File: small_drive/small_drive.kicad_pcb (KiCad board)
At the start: 2 copper layers, 83.8 x 71.8 mm, 143 parts, among them CON1 BARREL_JACK, J1 DB9, M1 SiR826DP, M2 SiR826DP, M3 SiR826DP, M4 SiR826DP, M5 SiR826DP, M6 SiR826DP, M7 SiR826DP, P1 CONN_01X04, P10 CONN_01X02, P11 CONN_01X02, P12 CONN_01X02, P13 CONN_01X04, P14 CONN_01X02, P2 CONN_01X04, P3 CONN_01X06, P4 CONN_01X08, P5 CONN_01X02, P6 CONN_01X02, P7 CONN_01X02, P8 CONN_01X02, P9 CONN_01X04, U1 STM32F334K8, U10 LM5106, U11 ACS711ELCTR-25AB-T, U12 ACS711ELCTR-25AB-T, U13 ACS711ELCTR-25AB-T, U14 STM32F030F4P6TR, U15 LTC2850, U16 LIS3LV02DQ, U17 STM32F030F4P6TR, U18 LTC2850, U19 LIS3LV02DQ, U2 OKR_T3, U20 DS28CM00, U21 DS28CM00, U22 TL431, U23 LT3012, U24 STM32F030F4P6TR, U25 MC33074DTBR2, U3 LTC2850, U4 LTC2850, U5 LTC2850, U6 LT1764EQ, U7 MC33074DTBR2, U8 LM5106, U9 LM5106

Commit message: Before splitting.
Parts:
- added C48: C, Capacitors_SMD:C_0603, B.Cu at (108.2, 88.5)
- added C49: C, Capacitors_SMD:C_0603, B.Cu at (108.2, 87.0)
- added Y1: Crystal, Crystals:QC3CA, B.Cu at (111.8, 88.5)
- moved C16 3.18 mm to (108.2, 90.0), turned to 180 degrees
- moved P13 1.50 mm to (170.5, 112.3)
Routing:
- net Net-(C49-Pad2): track 0.00 -> 9.74 mm
- net Net-(C48-Pad2): track 0.00 -> 8.62 mm
- net /A: track 37.8 -> 43.8 mm
- net /B: track 33.8 -> 39.4 mm
- net /pomp/Vdd: track 76.6 -> 81.8 mm
- net /Z: track 31.4 -> 36.5 mm
- net GND: track 365.1 -> 369.6 mm
- net +12V: track 139.5 -> 143.8 mm
- net /pomp/SWCLK: track 11.6 -> 12.8 mm
- net /pomp/Vss: track 169.0 -> 169.7 mm
- net Net-(C47-Pad1): track 2.66 -> 3.32 mm
- net /pomp/SWDIO: track 9.94 -> 10.6 mm
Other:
- board text added: "0"
- board text added: "0 D C +3.3"
- board text added: "SWD C,D"

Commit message: PCB ordered
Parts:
- removed C10, C11, C28, C29, C30, C31, C32, C33, C34, C35, C36, C37, C38, C40, C42, C43, C44: 100nF, Capacitors_SMD:C_0603
- removed C39: 470uF/63V, Capacitors_ThroughHole:C_Radial_D16_L25_P7.5
- removed C41: 100uF/35V, Capacitors_SMD:c_elec_8x10.5
- removed C45: 1uF/100V, Capacitors_SMD:C_1206
- removed C46: C, Capacitors_SMD:C_0603
- removed D5, D6, D7, D8: STPS2150A, Diodes_SMD:SMA_Standard
- removed HOLE5, HOLE6, HOLE7, HOLE8: HOLE, Mounting_Holes:MountingHole_3mm
- removed M7: SiR826DP, 00_Passives:SOT-669_GDS
- removed P1, P9: CONN_01X04, Pin_Headers:Pin_Header_Angled_1x04
- removed P10, P8: CONN_01X02, Pin_Headers:Pin_Header_Straight_1x02
- removed P11, P12, P14: CONN_01X02, 00_Passives:Wiecon_25.197.0253.0
- removed P13: CONN_01X04, Pin_Headers:Pin_Header_Straight_1x04
- removed R18, R19: R, Resistors_SMD:R_0603
- removed R20: 1.5k, Resistors_SMD:R_0603
- removed R21: 300, Resistors_SMD:R_0603
- removed R22: 910, Resistors_SMD:R_0603
- removed R23, R29, R30, R31: 1k, Resistors_SMD:R_0603
- removed R24: 3.0k, Resistors_SMD:R_0603
- removed R25: 1.8k, Resistors_SMD:R_0603
- removed R26: 51k, Resistors_SMD:R_0603
- removed R27: 2.2k, Resistors_SMD:R_0603
- removed R28: R, Resistors_SMD:R_2512
- removed U14, U17, U24: STM32F030F4P6TR, Housings_SSOP:TSSOP-20_4.4x6.5mm_Pitch0.65mm
- removed U15, U18: LTC2850, Housings_SOIC:SOIC-8_3.9x4.9mm_Pitch1.27mm
- removed U16, U19: LIS3LV02DQ, Housings_DFN_QFN:QFN-28-1EP_7x7mm_Pitch0.8mm
- removed U20, U21: DS28CM00, 00_Passives:SOT23_5
- removed U22: TL431, TO_SOT_Packages_SMD:SOT-23
- removed U23: LT3012, Housings_SSOP:TSSOP-16-1EP_4.4x5mm_Pitch0.65mm
- removed U25: MC33074DTBR2, Housings_SSOP:TSSOP-14_4.4x5mm_Pitch0.65mm
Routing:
- net /pomp/Vss: track 169.7 -> 0.00 mm, vias 1 -> 0
- net /pomp/Vdd: track 81.8 -> 0.00 mm, vias 1 -> 0
- net /g_sensor2/Vss: track 79.3 -> 0.00 mm, vias 2 -> 0
- net /g_sensor1/Vss: track 79.3 -> 0.00 mm, vias 2 -> 0
- net /pomp/Vpower: track 69.4 -> 0.00 mm
- net /g_sensor1/Vdd: track 59.6 -> 0.00 mm, vias 2 -> 0
- net /g_sensor2/Vdd: track 59.6 -> 0.00 mm, vias 2 -> 0
- net /pomp/MAINS: track 39.0 -> 0.00 mm
- net /pomp/CURRENT: track 16.0 -> 0.00 mm
- net Net-(C38-Pad1): track 14.3 -> 0.00 mm
- net Net-(D7-PadA): track 13.8 -> 0.00 mm
- net /pomp/SWCLK: track 12.8 -> 0.00 mm
- net Net-(M7-PadS): track 12.5 -> 0.00 mm
- net /pomp/SWDIO: track 10.6 -> 0.00 mm
- net Net-(R26-Pad2): track 10.4 -> 0.00 mm
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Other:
- board size 83.8 x 71.8 mm -> 58.8 x 71.8 mm
- board text removed: "0"
- board text removed: "0 D C +3.3"
- board text removed: "SWD C,D"

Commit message: Pauze klus.
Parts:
- removed CON1: BARREL_JACK, 00_Passives:smd_barrel_jack
- removed P4: CONN_01X08, Connectors_Molex:Molex_PicoBlade_53261-0871
- added C10: 100nF, Capacitors_SMD:C_0603, F.Cu at (68.5, 79.2)
- added C11: 100nF, Capacitors_SMD:C_0603, F.Cu at (71.0, 76.8)
- added C28: 100nF, Capacitors_SMD:C_0603, F.Cu at (72.5, 83.2)
- added C29: 100nF, Capacitors_SMD:C_0603, F.Cu at (75.0, 80.2)
- added C30: 10uF, Capacitors_SMD:C_1210, F.Cu at (68.2, 75.0)
- added C31: 10uF, Capacitors_SMD:C_1210, F.Cu at (75.0, 85.2)
- added C32: 100uF/35V, Capacitors_SMD:c_elec_8x10.5, F.Cu at (69.0, 59.0)
- added C33: 100nF, Capacitors_SMD:C_0603, B.Cu at (72.2, 56.2)
- added C34: 100uF/35V, Capacitors_SMD:c_elec_8x10.5, F.Cu at (114.0, 53.5)
- added C35: 10nF, Capacitors_SMD:C_0603, F.Cu at (113.0, 68.2)
- added C36: 100uF/35V, Capacitors_SMD:c_elec_8x10.5, F.Cu at (125.0, 53.5)
- added C37: 100nF, Capacitors_SMD:C_0603, F.Cu at (107.2, 59.0)
- added C38: 100uF/35V, Capacitors_SMD:c_elec_8x10.5, F.Cu at (67.8, 116.5)
- added C39: 100nF, Capacitors_SMD:C_0603, F.Cu at (107.0, 76.0)
- added C40: 100nF, Capacitors_SMD:C_0603, F.Cu at (107.0, 94.5)
- added C41: 100nF, Capacitors_SMD:C_0603, F.Cu at (107.0, 113.0)
- added C42: 100nF, Capacitors_SMD:C_0603, F.Cu at (75.5, 88.5)
- added C43: 100nF, Capacitors_SMD:C_0603, F.Cu at (98.5, 95.5)
- added C44: 2.2uF, Capacitors_SMD:C_1206, B.Cu at (74.8, 95.0)
- added C45: 100nF, Capacitors_SMD:C_0603, F.Cu at (72.2, 91.2)
- added C46: 25pF, Capacitors_SMD:C_0603, F.Cu at (67.0, 91.0)
- added C50: 100nF, Capacitors_SMD:C_0603, B.Cu at (69.8, 102.8)
- added C51: 100nF, Capacitors_SMD:C_0603, B.Cu at (69.8, 99.0)
- added C52: 100nF, Capacitors_SMD:C_0603, F.Cu at (116.2, 125.0)
- added C53: 100nF, Capacitors_SMD:C_0603, F.Cu at (116.2, 82.2)
- added C54: 100nF, Capacitors_SMD:C_0603, F.Cu at (116.2, 100.8)
- added C55: 100nF, Capacitors_SMD:C_0603, F.Cu at (116.2, 119.2)
- added C56: 100nF, Capacitors_SMD:C_0603, F.Cu at (32.4, 67.6)
- added C57: 100nF, Capacitors_SMD:C_0603, B.Cu at (57.8, 102.5)
- added C58: 100nF, Capacitors_SMD:C_0603, F.Cu at (37.5, 67.6)
- added C59: 100nF, Capacitors_SMD:C_0603, B.Cu at (66.2, 66.8)
- added J2: DB15, Connectors_Amphenol:DB15F_HD20_SIZE2, F.Cu at (58.0, 68.8)
- added P1: CONN_01X04, Connect:bornier4, F.Cu at (78.0, 130.5)
- added R18: 510, Resistors_SMD:R_0603, B.Cu at (59.8, 81.2)
- added R19: 1k, Resistors_SMD:R_0603, B.Cu at (54.5, 60.0)
- added R20: 1k, Resistors_SMD:R_0603, B.Cu at (61.5, 67.0)
- added R21: R, Resistors_SMD:R_0603, B.Cu at (61.8, 70.2)
- added R22: R, Resistors_SMD:R_0603, B.Cu at (62.5, 57.5)
- added R23: R, Resistors_SMD:R_0603, B.Cu at (62.5, 63.2)
- added R24: R, Resistors_SMD:R_0603, B.Cu at (58.2, 100.0)
- added R25: 1k, Resistors_SMD:R_0603, F.Cu at (100.2, 73.0)
- added R26: 1k, Resistors_SMD:R_0603, F.Cu at (102.0, 73.0)
- added R27: 510, Resistors_SMD:R_0603, F.Cu at (103.8, 73.0)
- added R28: 510, Resistors_SMD:R_0603, F.Cu at (105.5, 73.0)
- added R29: 680, Resistors_SMD:R_0603, F.Cu at (106.2, 131.5)
- added R30: 680, Resistors_SMD:R_0603, F.Cu at (106.2, 128.0)
- added R31: 680, Resistors_SMD:R_0603, F.Cu at (106.2, 129.8)
- added R33: 300, Resistors_SMD:R_0603, F.Cu at (114.5, 68.2)
- added R34: 56k, Resistors_SMD:R_0603, F.Cu at (114.5, 71.0)
- added R35: 6.49k, Resistors_SMD:R_0603, F.Cu at (67.0, 89.2)
- added R36: 220, Resistors_SMD:R_0603, B.Cu at (73.2, 92.5)
- added R37: 220, Resistors_SMD:R_0603, B.Cu at (81.0, 94.5)
- added R38: R, Resistors_SMD:R_0603, B.Cu at (57.8, 105.2)
- added R39: R, Resistors_SMD:R_0603, B.Cu at (50.8, 109.0)
- added R40: R, Resistors_SMD:R_0603, B.Cu at (49.8, 94.8)
- added R41: R, Resistors_SMD:R_0603, B.Cu at (54.0, 109.0)
- added R42: R, Resistors_SMD:R_0603, B.Cu at (55.0, 110.8)
- added R43: R, Resistors_SMD:R_0603, B.Cu at (49.8, 96.5)
- added R44: 22, Resistors_SMD:R_0603, B.Cu at (79.8, 84.2)
- added R45: 22, Resistors_SMD:R_0603, B.Cu at (79.8, 82.5)
- added R46: R, Resistors_SMD:R_0603, B.Cu at (74.2, 123.5)
- added U14: AD8226, Housings_SOIC:SOIC-8_3.9x4.9mm_Pitch1.27mm, B.Cu at (67.8, 63.2)
- added U15: MAX3096, Housings_SOIC:SOIC-16_3.9x9.9mm_Pitch1.27mm, B.Cu at (53.0, 102.8)
- added U16: AMC1203, 00_Passives:SO8_11, F.Cu at (105.5, 68.2)
- added U17: 7805, 00_Local:TO220_78xx, F.Cu at (124.8, 62.8)
- added U18: LT1764EQ, 00_Passives:DD-PAK, B.Cu at (66.2, 119.2)
- added U19: KSZ8081, Housings_DFN_QFN:QFN-24-1EP_4x4mm_Pitch0.5mm, B.Cu at (69.8, 91.0)
- added U20: ETH100_MAG, 00_Passives:ETH100_MAG, F.Cu at (68.1, 106.5)
- added X1: NKE1212DC, 00_Local:NKE-SC, F.Cu at (76.0, 55.0)
- added X2: NKE1212DC, 00_Local:NKE-SC, F.Cu at (111.5, 63.5)
- added X3: HCPL0201, Housings_SOIC:SOIC-8_3.9x4.9mm_Pitch1.27mm, F.Cu at (111.5, 82.2)
- added X4: HCPL0201, Housings_SOIC:SOIC-8_3.9x4.9mm_Pitch1.27mm, F.Cu at (111.5, 119.2)
- added X5: HCPL0201, Housings_SOIC:SOIC-8_3.9x4.9mm_Pitch1.27mm, F.Cu at (111.5, 100.8)
- added X6: HCPL0201, Housings_SOIC:SOIC-8_3.9x4.9mm_Pitch1.27mm, F.Cu at (111.5, 125.0)
- added Y2: 25MHz, Crystals:crystal_FA238-TSX3225, F.Cu at (64.0, 91.8)
- C13, C15, C16, C17, C18, C8, C9, R10, R11, R12, R13, R14, R6, R7, R8, R9, U12, U7: moved to F.Cu
- C47: value 100nF -> 25pF
- C48, C49: value C -> 15pF
- J1: footprint Connect:DB9FC -> Connectors_Amphenol:DB9FC_HD-20
- M1, M2, M3, M4, M5, M6: footprint 00_Passives:SOT-669_GDS -> 00_Passives:SOT-669_GDS_therma
- P3: value CONN_01X06 -> CONN_01X04; footprint Connectors_Molex:Molex_PicoBlade_53261-0671 -> Pin_Headers:Pin_Header_Straight_1x04; moved to F.Cu
- R1: value 270 -> 10k; moved to F.Cu
- R15, R16, R17: value R -> 10k
- R32: value 0 -> 680
- U1: value STM32F334K8 -> XMC4400-F64x512; footprint Housings_QFP:LQFP-32_7x7mm_Pitch0.8mm -> Housings_QFP:LQFP-64-1EP_10x10mm_Pitch0.5mm
- U11, U13: value ACS711ELCTR-25AB-T -> ACS711KLCTR-12AB-T; moved to F.Cu
- U2: value OKR_T3 -> ips511g; footprint 00_Passives:okr_t3 -> Housings_SOIC:SOIC-8_3.9x4.9mm_Pitch1.27mm; moved to B.Cu
- U3: value LTC2850 -> ips511g
- U5: value LTC2850 -> AD8226
- Y1: value Crystal -> 12MHz
- moved C17 87.5 mm to (68.5, 81.2)
- moved C3 79.0 mm to (50.8, 61.8), turned to 0 degrees
- moved C1 77.5 mm to (69.0, 68.0)
- moved U2 72.2 mm to (52.2, 71.0), turned to 180 degrees
- moved C18 71.3 mm to (75.0, 82.2), turned to 180 degrees
- moved C15 68.1 mm to (71.0, 83.2), turned to 90 degrees
- moved U5 63.7 mm to (67.8, 57.5), turned to 0 degrees
- moved C7 62.3 mm to (50.8, 74.5), turned to 0 degrees
- moved U3 55.6 mm to (52.2, 65.4)
- moved C14 55.1 mm to (67.8, 135.0), turned to 0 degrees
- moved J1 53.9 mm to (55.8, 127.9), turned to 270 degrees
- moved R1 53.2 mm to (68.5, 77.5), turned to 180 degrees
- moved C8 50.0 mm to (72.5, 76.8), turned to 270 degrees
- moved Y1 49.3 mm to (62.8, 82.8)
- moved U4 49.3 mm to (66.5, 70.2)
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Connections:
- C19 pad 1: GND -> GNDPWR
- C19 pad 2: +12V -> +12P
- C2 pad 2: GND -> GNDPWR
- C20 pad 1: GND -> GNDPWR
- C20 pad 2: +12V -> +12P
- C21 pad 1: GND -> GNDPWR
- C21 pad 2: +12V -> +12P
- C25 pad 2: GND -> GNDPWR
- C26 pad 2: GND -> GNDPWR
- C27 pad 2: GND -> GNDPWR
- C4 pad 2: GND -> GNDPWR
- C48 pad 1: GND -> Net-(C48-Pad1)
- C48 pad 2: Net-(C48-Pad2) -> GND
- C5 pad 2: GND -> GNDPWR
- C9 pad 1: +5V -> +3.3V
- D2 pad A: +12V -> +12P
- D3 pad A: +12V -> +12P
- D4 pad A: +12V -> +12P
- M2 pad S: GND -> GNDPWR
- M4 pad S: GND -> GNDPWR
- M6 pad S: GND -> GNDPWR
- P2 pad 1: +5V -> +3.3V
- P2 pad 2: /SWDAT -> Net-(P2-Pad2)
- P2 pad 3: /SWCLK -> Net-(P2-Pad3)
- P3 pad 1: GND -> /LED0
- P3 pad 2: GND -> /LED1
- P3 pad 3: Net-(P3-Pad3) -> /LED2
- P3 pad 4: Net-(P3-Pad4) -> /LED3
- P5 pad 1: +60V -> /M0
- P5 pad 2: /M0 -> +60V
- P6 pad 1: GND -> /M1
- P6 pad 2: /M1 -> GNDPWR
- P7 pad 1: GND -> /M2
- P7 pad 2: /M2 -> GNDPWR
- R1 pad 1: Net-(R1-Pad1) -> +3.3V
- R1 pad 2: GND -> Net-(R1-Pad2)
- R12 pad 1: +3.3V -> +3.3VADC
- R15 pad 2: GND -> GNDPWR
- R16 pad 2: GND -> GNDPWR
- R17 pad 2: GND -> GNDPWR
- R2 pad 1: Net-(D1-Pad6) -> Net-(D1-Pad8)
- R3 pad 1: Net-(D1-Pad8) -> Net-(D1-Pad2)
- R32 pad 1: +3.3V -> Net-(R32-Pad1)
- R32 pad 2: Net-(J1-Pad4) -> /HBEN
- R4 pad 1: Net-(D1-Pad2) -> Net-(D1-Pad6)
- R6 pad 1: +3.3V -> +3.3VADC
- R9 pad 1: +3.3V -> +3.3VADC
- U1 pad 1: +3.3V -> /ETH_CRS_DVA
- U1 pad 10: /CUR1 -> Net-(U1-Pad10)
- U1 pad 11: /CUR2 -> Net-(U1-Pad11)
- U1 pad 12: /LED0 -> Net-(U1-Pad12)
- U1 pad 13: /LED1 -> +3.3V
- U1 pad 14: /LED2 -> /ENC_SIN
- U1 pad 15: /LED3 -> /ENC_SIN
- U1 pad 16: GND -> /ENC_COS
- U1 pad 17: +3.3V -> Net-(U1-Pad17)
- U1 pad 18: /HB0 -> /CUR2
- U1 pad 19: /HB1 -> Net-(U1-Pad19)
- U1 pad 2: Net-(C48-Pad2) -> /ENC_RXD2
- U1 pad 20: /HB2 -> /CUR0
- U1 pad 21: /HBEN -> GND
- U1 pad 22: /DXD -> +3.3VADC
- U1 pad 23: /SWDAT -> Net-(U1-Pad23)
- U1 pad 24: /SWCLK -> /CUR1
- U1 pad 25: /ENC_RXD -> /VddC
- U1 pad 26: /ENC_TXD -> +3.3V
- U1 pad 27: Net-(U1-Pad27) -> /ETH0_TXD1
- U1 pad 28: /DXD -> /ETH0_TXD0
- U1 pad 29: /TXD -> /ETH0_TX_EN
- U1 pad 3: Net-(C49-Pad2) -> /LED2
- U1 pad 30: /RXD -> /ETH0_RXERA
- U1 pad 31: GND -> /ETH0_RXD1A
- U1 pad 32: GND -> /ETH0_RXD0A
- U1 pad 4: Net-(C47-Pad1) -> /LED3
- U1 pad 5: +3.3V -> Net-(U1-Pad5)
- U1 pad 6: /A -> Net-(U1-Pad6)
- U1 pad 7: /B -> Net-(U1-Pad7)
- U1 pad 8: /Z -> +3.3V
- U1 pad 9: /CUR0 -> /VddC
- U10 pad 1: +12V -> +12P
- U10 pad 7: /HBEN -> Net-(U10-Pad7)
- U10 pad 8: /HB2 -> Net-(U10-Pad8)
- U10 pad 9: GND -> GNDPWR
- U11 pad 8: +3.3V -> +3.3VADC
- U12 pad 8: +3.3V -> +3.3VADC
- U13 pad 8: +3.3V -> +3.3VADC
- U2 pad 1: +12V -> GND
- U2 pad 2: +12V -> /ENC_5V
- U2 pad 4: +5V -> Net-(J2-Pad11)
- U2 pad 5: Net-(R1-Pad1) -> +5V
- U3 pad 1: /RXD -> GND
- U3 pad 2: /DXD -> /ENC_12V
- U3 pad 3: /DXD -> GND
- U3 pad 4: /TXD -> Net-(J2-Pad12)
- U3 pad 5: GND -> +12V
- U3 pad 6: Net-(P3-Pad3) -> +12V
- U3 pad 7: Net-(P3-Pad4) -> +12V
- U3 pad 8: +5V -> +12V
- U4 pad 1: Net-(U4-Pad1) -> /ENC_RXD
- U4 pad 2: +5V -> /ENC_DIR
- U4 pad 3: +5V -> /ENC_DIR
- U4 pad 8: +5V -> +3.3V
- U5 pad 1: /ENC_RXD -> Net-(J2-Pad15)
- U5 pad 2: GND -> Net-(R22-Pad1)
- U5 pad 3: GND -> Net-(R22-Pad2)
- U5 pad 4: GND -> Net-(J2-Pad8)
- U5 pad 5: GND -> -12V
- U5 pad 6: Net-(P4-Pad2) -> GND
- U5 pad 8: +5V -> +12V
- U6 pad 1: Net-(U6-Pad1) -> +5V
- U7 pad 4: +3.3V -> +3.3VADC
- U8 pad 1: +12V -> +12P
- U8 pad 7: /HBEN -> Net-(U10-Pad7)
- U8 pad 8: /HB0 -> Net-(U8-Pad8)
- U8 pad 9: GND -> GNDPWR
- U9 pad 1: +12V -> +12P
- U9 pad 7: /HBEN -> Net-(U10-Pad7)
- U9 pad 8: /HB1 -> Net-(U9-Pad8)
- U9 pad 9: GND -> GNDPWR
- Y1 pad 1: Net-(C48-Pad2) -> Net-(C48-Pad1)
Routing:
- net GND: track 369.6 -> 222.9 mm, vias 38 -> 4
- net +3.3V: track 216.0 -> 77.8 mm, vias 7 -> 6
- net +12V: track 143.8 -> 5.71 mm, vias 1 -> 0
- net +5P: track 0.00 -> 115.9 mm
- net +3.3VADC: track 0.00 -> 105.0 mm, vias 0 -> 1
- net +5V: track 89.2 -> 5.59 mm
- net /HBEN: track 72.6 -> 0.00 mm, vias 4 -> 0
- net GNDPWR: track 0.00 -> 65.5 mm, vias 0 -> 3
- net Net-(U10-Pad7): track 0.00 -> 63.7 mm, vias 0 -> 3
- net Net-(R29-Pad1): track 0.00 -> 52.3 mm
- net +12P: track 0.00 -> 50.6 mm
- net /HB2: track 49.7 -> 0.00 mm, vias 2 -> 0
- net /~A: track 0.00 -> 46.9 mm
- net /ENC_B: track 0.00 -> 46.2 mm
- net /ENC_A: track 0.00 -> 43.0 mm
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- added copper zone on F.Cu, net +60V
- added copper zone on F.Cu, net /M0
- added copper zone on F.Cu, net /M1
- added copper zone on F.Cu, net /M2
- added copper zone on F.Cu, net /SW0
- added copper zone on F.Cu, net /SW1
- added copper zone on F.Cu, net /SW2
- added copper zone on B.Cu, net GNDPWR
- removed copper zone on B.Cu, net /M0
- removed copper zone on B.Cu, net /M1
- removed copper zone on B.Cu, net /M2
- removed copper zone on B.Cu, net GND
- removed copper zone on F.Cu, net GND
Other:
- board size 58.8 x 71.8 mm -> 100 x 100 mm
- board text removed: "GND SWCLK SWDAT +5V"
- board text removed: "SMALL_DRIVE v1.0"

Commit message: Pauze backup
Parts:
- added P4: CONN_01X04, Pin_Headers:Pin_Header_Straight_1x04, F.Cu at (47.0, 140.9)
- added P8: CONN_01X01, Pin_Headers:Pin_Header_Straight_1x01, F.Cu at (41.2, 148.8)
- added R47: 10k, Resistors_SMD:R_0603, F.Cu at (59.5, 151.2)
- added R48: 10k, Resistors_SMD:R_0603, F.Cu at (63.2, 153.8)
- C13, C35, C37, C43, C58, R25, R26, R27, R28, R33, R34, U16, Y2: moved to B.Cu
- P1: footprint Connect:bornier4 -> 00_Passives:PC_drive_5.25_conn
- moved C3 121.4 mm to (65.2, 182.2), turned to 90 degrees
- moved C58 118.3 mm to (77.6, 178.9), turned to 90 degrees
- moved HOLE3 117.2 mm to (42.0, 107.0), turned to 90 degrees
- moved HOLE4 116.7 mm to (42.0, 165.0), turned to 90 degrees
- moved U3 115.0 mm to (61.5, 180.0), turned to 270 degrees
- moved R22 112.4 mm to (53.0, 169.5), turned to 180 degrees
- moved R19 111.2 mm to (61.5, 171.0), turned to 180 degrees
- moved R21 109.6 mm to (75.8, 178.9), turned to 90 degrees
- moved U2 109.1 mm to (56.0, 180.0), turned to 270 degrees
- moved U4 108.8 mm to (71.3, 178.9), turned to 0 degrees
- moved R20 108.7 mm to (54.2, 175.5), turned to 180 degrees
- moved C59 108.7 mm to (124.5, 158.5), turned to 180 degrees
- moved C56 108.1 mm to (83.2, 163.0), turned to 180 degrees
- moved U5 107.8 mm to (53.0, 164.2), turned to 90 degrees
- moved C7 107.3 mm to (52.5, 181.8), turned to 90 degrees
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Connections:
- R2 pad 1: Net-(D1-Pad8) -> Net-(D1-Pad4)
- R3 pad 1: Net-(D1-Pad2) -> Net-(D1-Pad6)
- R4 pad 1: Net-(D1-Pad6) -> Net-(D1-Pad2)
- R5 pad 1: Net-(D1-Pad4) -> Net-(D1-Pad8)
- U1 pad 53: /ENC_5V -> /ENC_12V
- U1 pad 59: /ENC_12V -> /ENC_5V
- U1 pad 60: /HB1 -> /HB2
- U1 pad 63: /HB2 -> /HB1
- U14 pad 6: GND -> Net-(U14-Pad6)
- U16 pad 2: Net-(C35-Pad1) -> GNDPWR
- U16 pad 3: GNDPWR -> Net-(C35-Pad1)
- U5 pad 6: GND -> Net-(U14-Pad6)
- U7 pad 5: GND -> Net-(R47-Pad2)
- U7 pad 6: GND -> Net-(U14-Pad6)
- U7 pad 7: Net-(U7-Pad7) -> Net-(U14-Pad6)
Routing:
- net +3.3V: track 77.8 -> 317.3 mm, vias 6 -> 14
- net +5V: track 5.59 -> 211.8 mm, vias 0 -> 2
- net +12V: track 5.71 -> 187.8 mm, vias 0 -> 3
- net GNDPWR: track 65.5 -> 143.0 mm, vias 3 -> 4
- net +12P: track 50.6 -> 122.3 mm
- net /ENC_RXD2: track 0.00 -> 65.8 mm
- net Net-(R32-Pad1): track 1.86 -> 55.6 mm
- net GND: track 222.9 -> 265.0 mm, vias 4 -> 50
- net Net-(R29-Pad1): track 52.3 -> 14.4 mm
- net /HBEN: track 0.00 -> 37.5 mm, vias 0 -> 1
- net /MDAT: track 5.68 -> 42.0 mm, vias 0 -> 2
- net /ETH0_~RST: track 0.00 -> 35.5 mm, vias 0 -> 2
- net /LED3: track 10.0 -> 45.5 mm
- net /ENC_5V: track 0.00 -> 33.7 mm
- net /A: track 41.2 -> 74.6 mm
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- added copper zone on B.Cu, net +3.3VADC
- added copper zone on B.Cu, net GND
- added copper zone on F.Cu, net GND
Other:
- board size 100 x 100 mm -> 100 x 80 mm

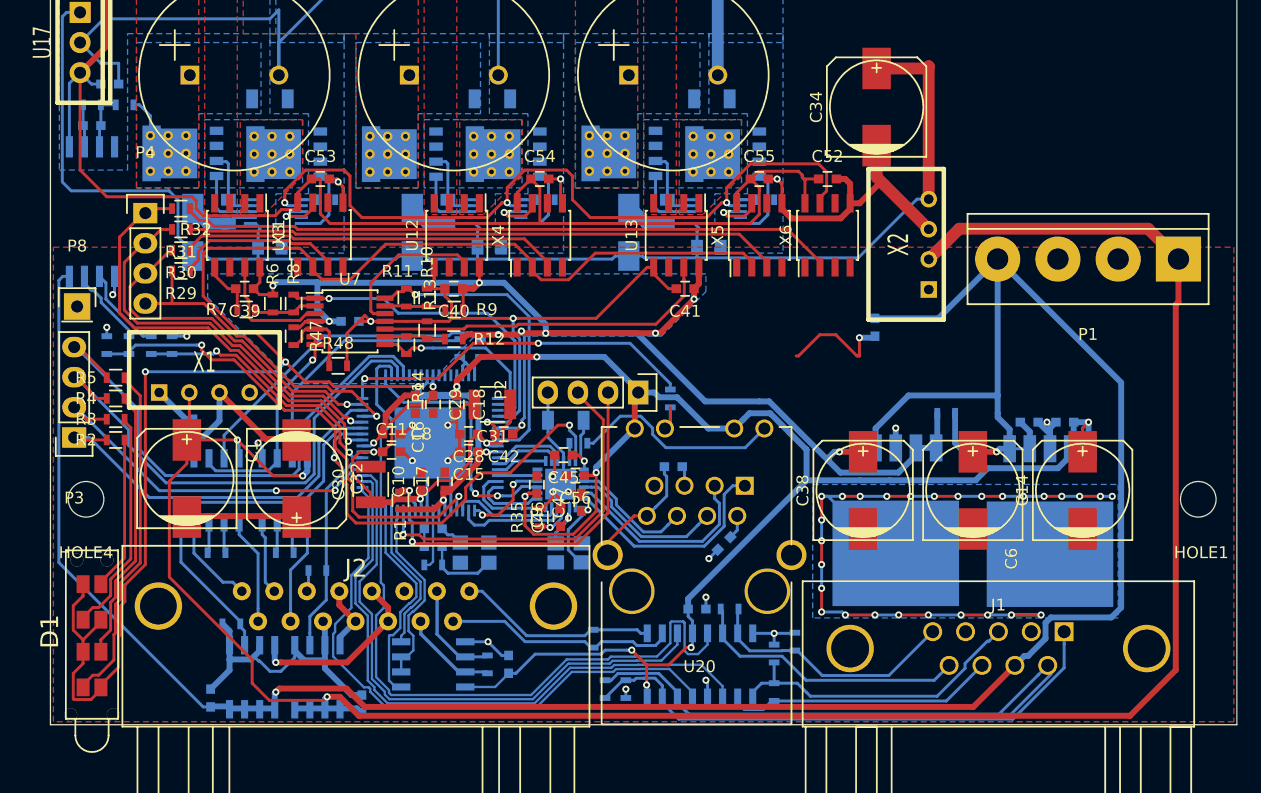
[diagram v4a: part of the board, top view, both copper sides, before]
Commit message: Moved enable opto.
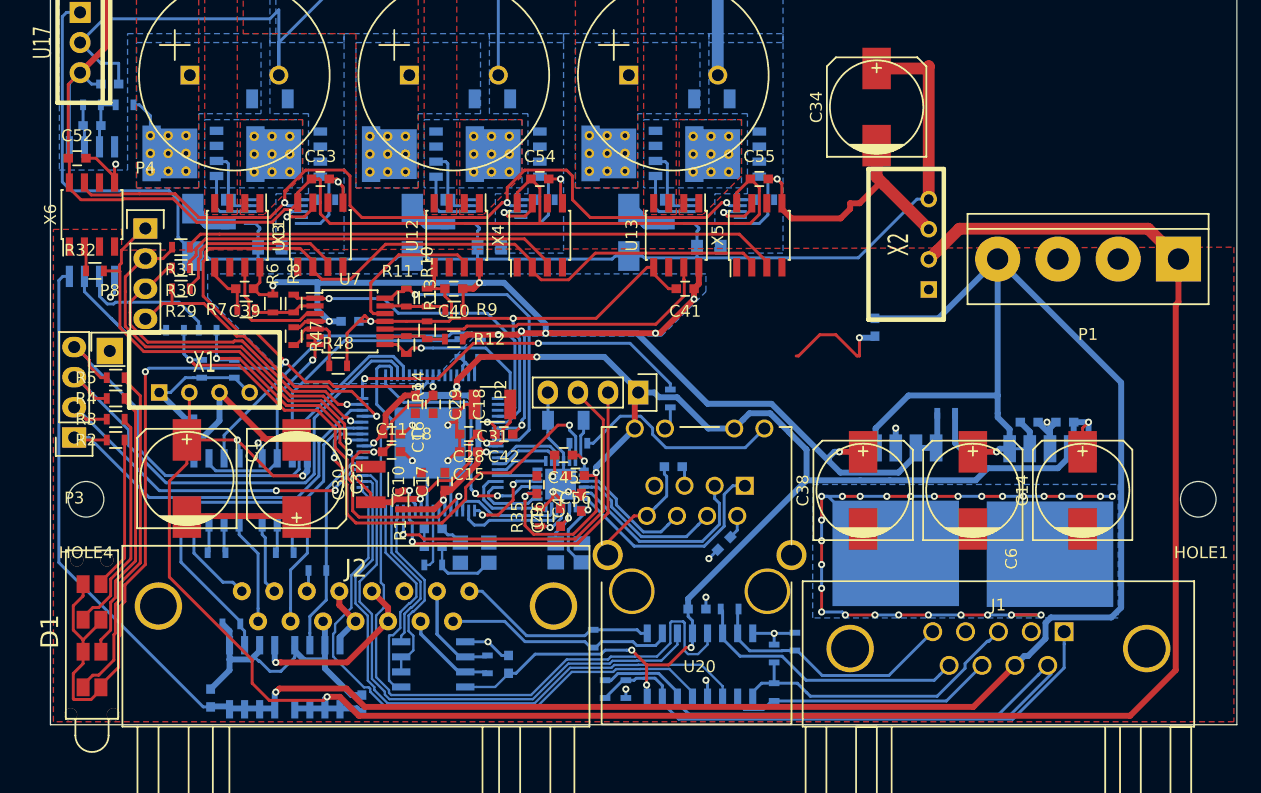
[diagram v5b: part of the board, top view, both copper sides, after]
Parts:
- moved C52 63.3 mm to (41.2, 136.2)
- moved X6 62.0 mm to (42.5, 141.0)
- moved R32 8.95 mm to (42.8, 145.8), turned to 0 degrees
- moved R28 8.25 mm to (51.8, 154.0), turned to 270 degrees
- moved R27 5.62 mm to (54.5, 154.0), turned to 270 degrees
- moved R26 4.91 mm to (52.2, 150.8), turned to 180 degrees
- moved P8 4.65 mm to (44.0, 152.5)
- moved R25 4.08 mm to (49.5, 150.8), turned to 180 degrees
- moved R29 1.50 mm to (50.0, 147.2)
- moved R30 1.50 mm to (50.0, 145.5)
- moved R31 1.50 mm to (50.0, 143.8)
- moved P4 1.29 mm to (47.0, 142.2)
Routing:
- net Net-(R32-Pad1): track 55.6 -> 2.11 mm
- net GND: track 265.0 -> 272.0 mm, vias 50 -> 48
- net +5P: track 114.1 -> 107.2 mm
- net Net-(U10-Pad7): track 65.5 -> 70.8 mm
- net Net-(R25-Pad2): track 6.70 -> 11.8 mm
- net /MDAT: track 42.0 -> 37.1 mm
- net Net-(R26-Pad2): track 7.26 -> 11.8 mm
- net GNDPWR: track 143.0 -> 145.1 mm, vias 4 -> 5
- net /MCLK: track 22.5 -> 20.6 mm
- net /HB0: track 28.2 -> 26.4 mm
- net /HBEN: track 37.5 -> 35.8 mm
- net Net-(R37-Pad2): track 3.95 -> 2.62 mm
- net Net-(R29-Pad1): track 14.4 -> 15.7 mm
- net Net-(R30-Pad1): track 32.1 -> 33.3 mm
- net /HB1: track 29.6 -> 29.1 mm

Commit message: PCB ordered.
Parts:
- moved C13 66.5 mm to (42.0, 148.0), turned to 0 degrees
- moved X2 6.04 mm to (107.0, 143.2)
- moved C34 3.91 mm to (104.8, 131.5), turned to 270 degrees
- moved R37 0.71 mm to (90.8, 156.0)
- moved R2 0.50 mm to (44.0, 160.0)
- moved R3 0.50 mm to (44.0, 158.2)
- moved R4 0.50 mm to (44.0, 156.5)
- moved R5 0.50 mm to (44.0, 154.8)
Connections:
- net Net-(P2-Pad2) renamed /SWDIO
- net Net-(P2-Pad3) renamed /SWCLK
- U1 pad 3: /LED2 -> /HBEN
- U1 pad 4: /LED3 -> /LED4
- U1 pad 52: /LED1 -> /ETH0_~RST
- U1 pad 57: /HBEN -> /ENC_5V
- U1 pad 58: /ETH0_~RST -> /LED0
- U1 pad 59: /ENC_5V -> /LED1
- U1 pad 62: /LED0 -> /LED2
- U1 pad 64: /LED4 -> /LED3
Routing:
- net +12P: track 122.3 -> 105.8 mm
- net +5V: track 211.8 -> 202.3 mm
- net +3.3V: track 317.4 -> 326.7 mm
- net GND: track 272.0 -> 263.9 mm, vias 48 -> 47
- net +3.3VADC: track 125.9 -> 117.9 mm
- net /LED2: track 43.2 -> 36.5 mm
- net Net-(J2-Pad2): track 15.1 -> 8.72 mm
- net Net-(J2-Pad10): track 14.2 -> 8.08 mm
- net /LED3: track 45.7 -> 39.6 mm
- net /LED4: track 30.7 -> 25.8 mm
- net /HBEN: track 35.8 -> 40.2 mm
- net /ETH0_~RST: track 35.5 -> 31.4 mm
- net Net-(R36-Pad1): track 17.9 -> 15.4 mm
- net /LED1: track 31.4 -> 33.7 mm, vias 2 -> 0
- net Net-(R25-Pad2): track 11.8 -> 10.2 mm
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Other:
- board text added: "GND SWCLK SWDIO +3.3V"
- board text added: "Small_drive v1.1"
- board text removed: "+"

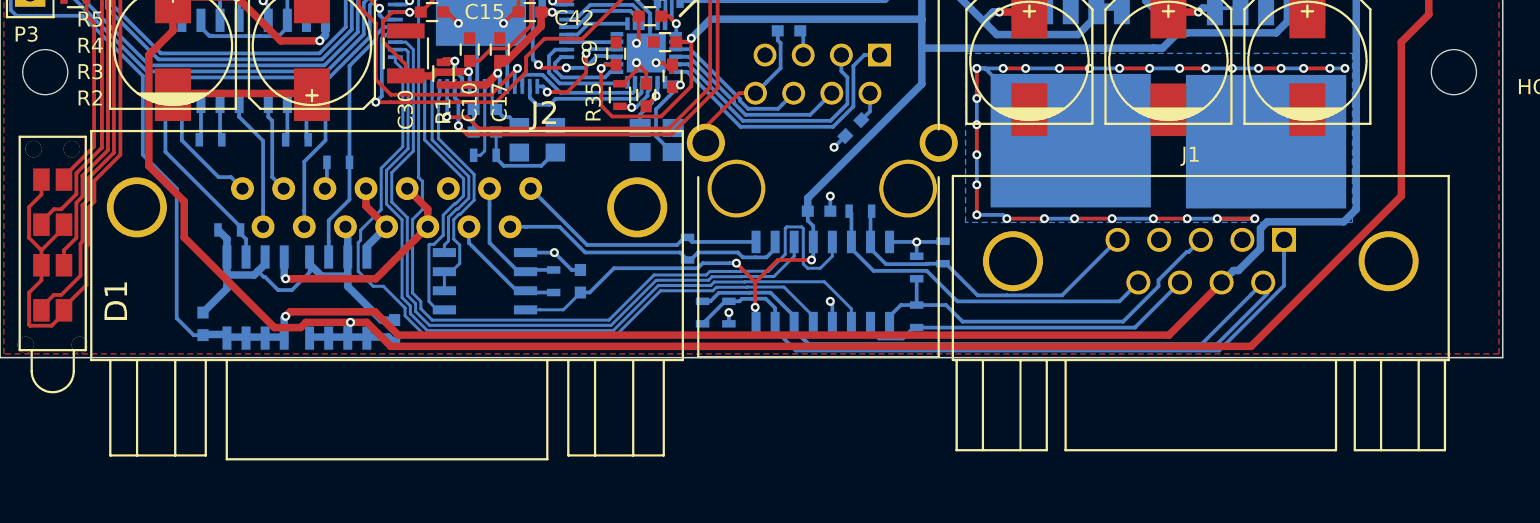
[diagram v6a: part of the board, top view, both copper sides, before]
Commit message: Header conversion in C++
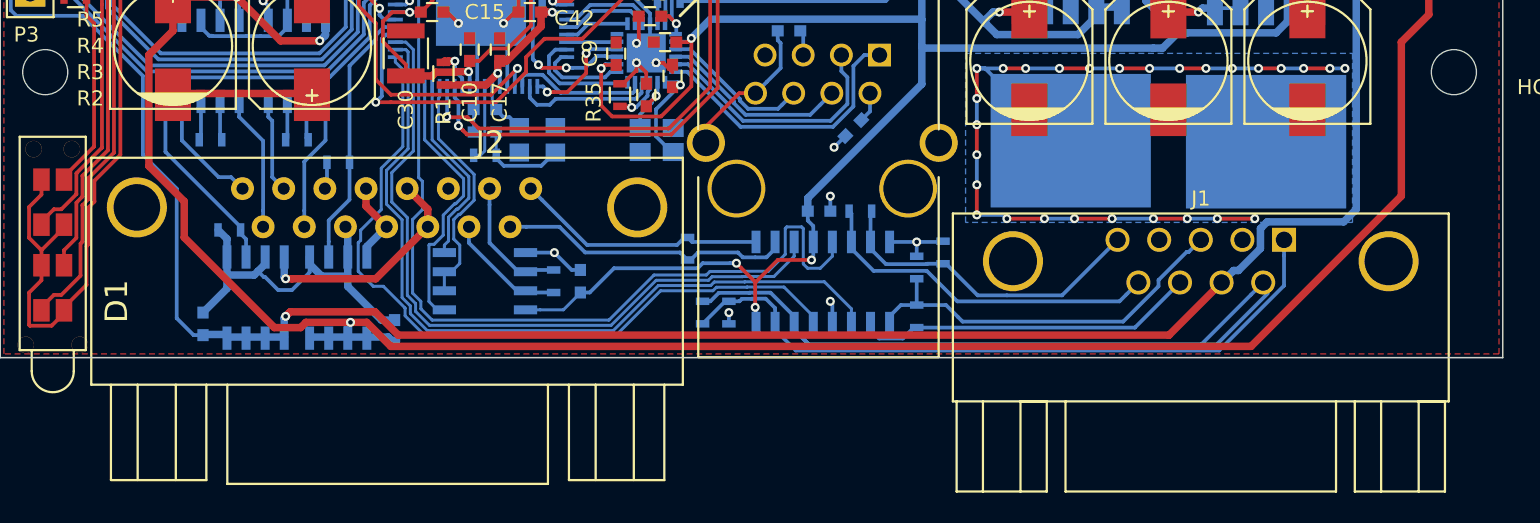
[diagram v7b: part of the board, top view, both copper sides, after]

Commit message: Functional PWM, including subsampling interrupt.
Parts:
- C46, C47: value 25pF -> 18pF
- C48, C49: value 15pF -> 12pF
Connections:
- net Net-(J2-Pad1) renamed /ENC_RXN
- net Net-(J2-Pad10) renamed /ENC_TXN
- net Net-(J2-Pad2) renamed /ENC_TXP
- net Net-(J2-Pad9) renamed /ENC_RXP
